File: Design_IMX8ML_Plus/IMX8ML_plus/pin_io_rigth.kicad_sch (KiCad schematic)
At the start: 2 parts, among them J3 DF40C-100DP-0.4V_51_, J4 DF40C-100DP-0.4V_51_

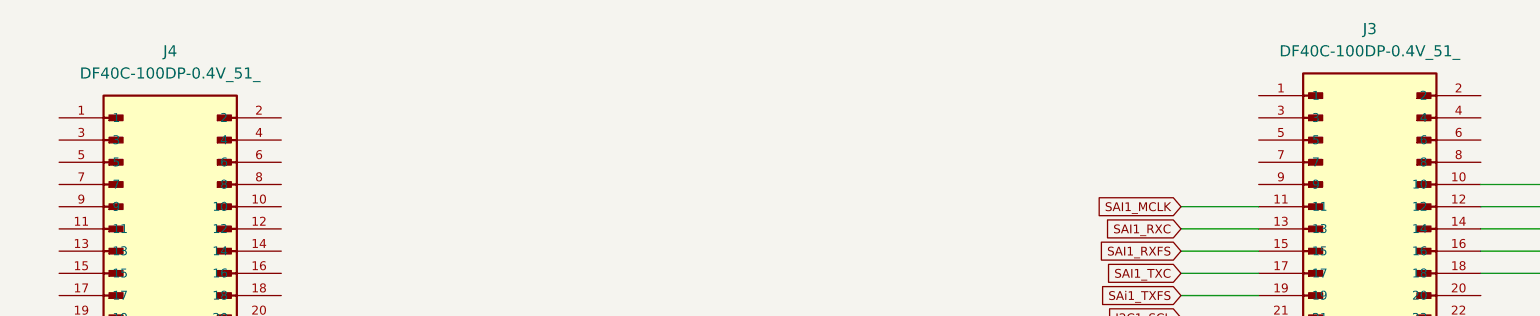
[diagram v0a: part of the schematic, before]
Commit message: Add SPB228 WIFI/BLE module
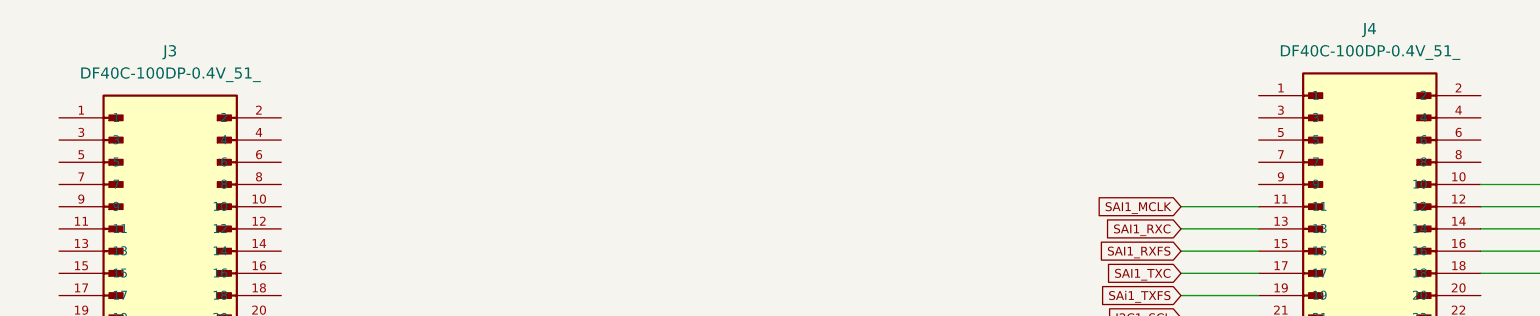
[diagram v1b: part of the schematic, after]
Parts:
- renumbered J4 to J3, J3 to J4

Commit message: CPU Board actualizate
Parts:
- J3: value DF40C-100DP-0.4V_51_ -> Front_Left
- J4: value DF40C-100DP-0.4V_51_ -> Back_Left
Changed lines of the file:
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@@
 			)
 		)
-		(property "Value" "DF40C-100DP-0.4V_51_"
+		(property "Value" "Front_Left"
 			(at 88.9 25.4 0)
 			(effects
@@
 			)
 		)
-		(property "Value" "DF40C-100DP-0.4V_51_"
+		(property "Value" "Back_Left"
 			(at 226.06 22.86 0)
 			(effects

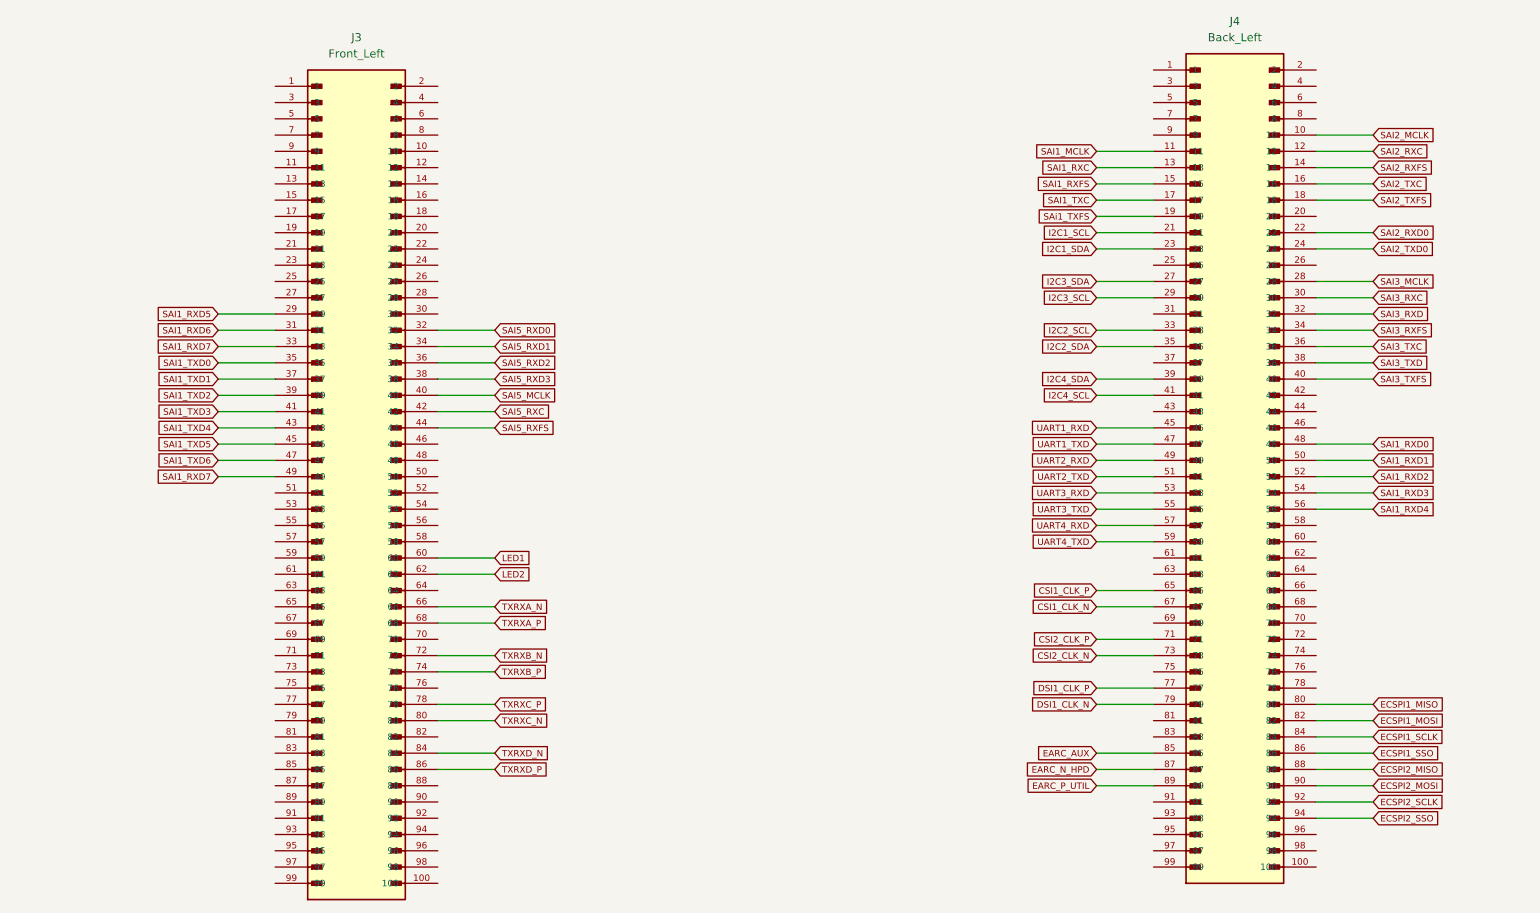
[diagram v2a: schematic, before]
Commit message: [IMX8ML-Processor] Reorganization of the pinout conector since processor to conectors
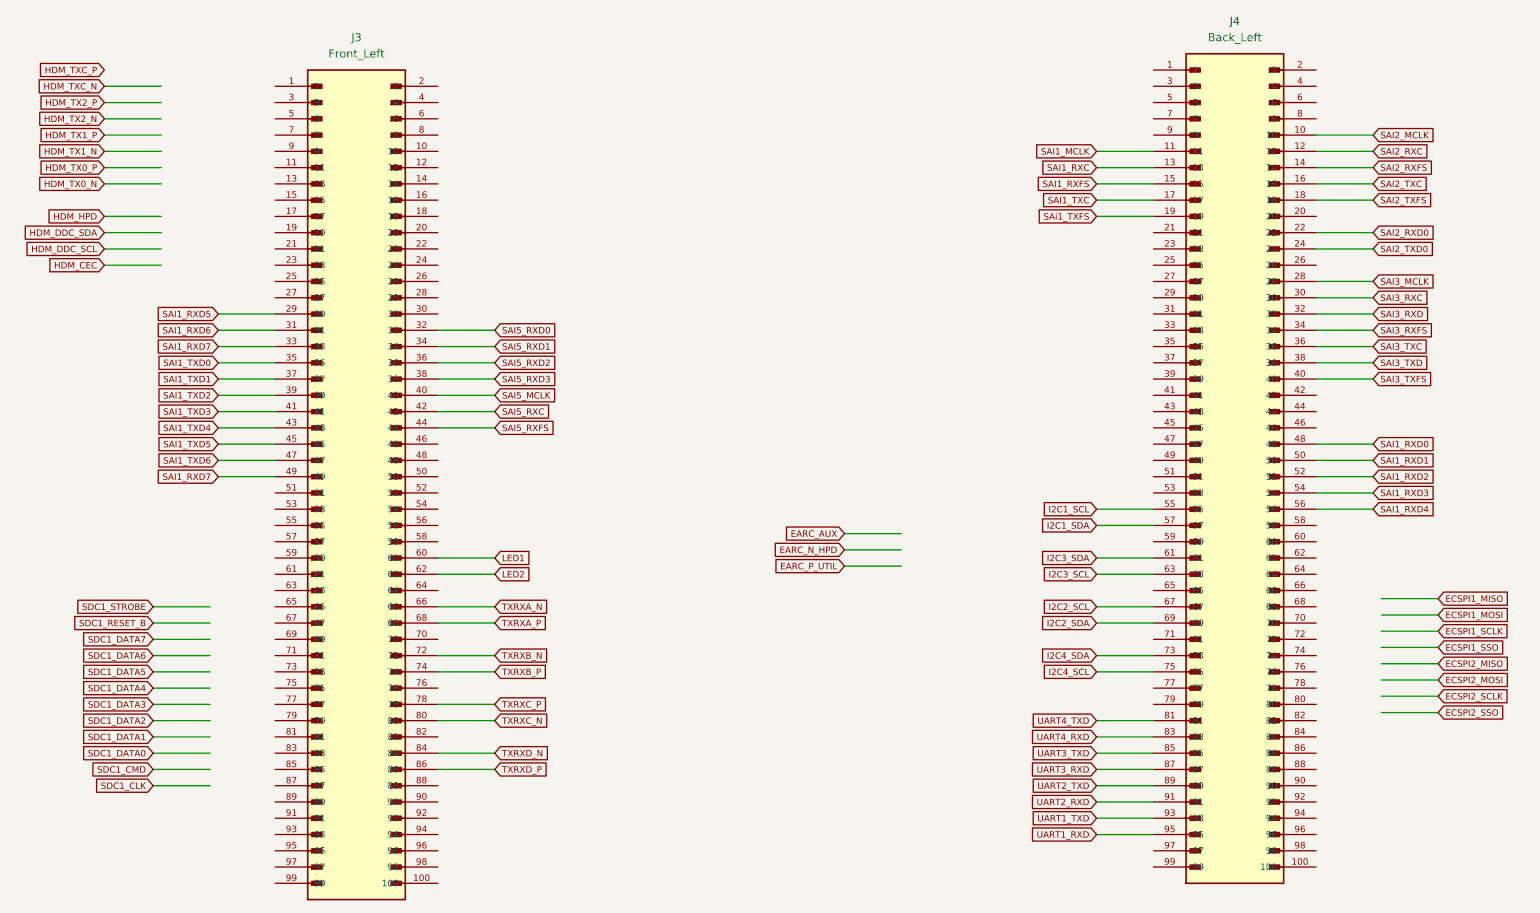
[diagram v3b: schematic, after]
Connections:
- net CSI1_CLK_N is gone; now on net I2C2_SCL: J4.67
- net CSI2_CLK_N is gone; now on net I2C4_SDA: J4.73
- net EARC_AUX: no longer J4.85
- net EARC_N_HPD: no longer J4.87
- net EARC_P_UTIL: no longer J4.89
- net ECSPI1_MISO: no longer J4.80
- net ECSPI1_MOSI: no longer J4.82
- net ECSPI1_SCLK: no longer J4.84
- net ECSPI1_SSO: no longer J4.86
- net ECSPI2_MISO: no longer J4.88
- net ECSPI2_MOSI: no longer J4.90
- net ECSPI2_SCLK: no longer J4.92
- net ECSPI2_SSO: no longer J4.94
- net I2C1_SCL: now also J4.55; no longer J4.21
- net I2C1_SDA: now also J4.57; no longer J4.23
- net I2C2_SCL: no longer J4.33
- net I2C2_SDA: now also J4.69; no longer J4.35
- net I2C3_SCL: now also J4.63; no longer J4.29
- net I2C3_SDA: now also J4.61; no longer J4.27
- net I2C4_SCL: now also J4.75; no longer J4.41
- net I2C4_SDA: no longer J4.39
- net UART1_RXD: now also J4.95; no longer J4.45
- net UART1_TXD: now also J4.93; no longer J4.47
- net UART2_RXD: now also J4.91; no longer J4.49
- net UART2_TXD: now also J4.89; no longer J4.51
- net UART3_RXD: now also J4.87; no longer J4.53
- net UART3_TXD: now also J4.85; no longer J4.55
- net UART4_RXD: now also J4.83; no longer J4.57
- net UART4_TXD: now also J4.81; no longer J4.59
- net CSI1_CLK_P: no longer names the net of J4.65
- net CSI2_CLK_P: no longer names the net of J4.71
- net DSI1_CLK_N: no longer names the net of J4.79
- net DSI1_CLK_P: no longer names the net of J4.77
